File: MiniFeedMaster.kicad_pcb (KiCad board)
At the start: 2 copper layers, 58.4 x 83.2 mm, 120 parts, among them J1 SWD, J2 CAN, J3 UART, J4 USB, J5 Feeder, J6 Chain, J7 VIn, J8 I2C, J9 EXT, SW1 Button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

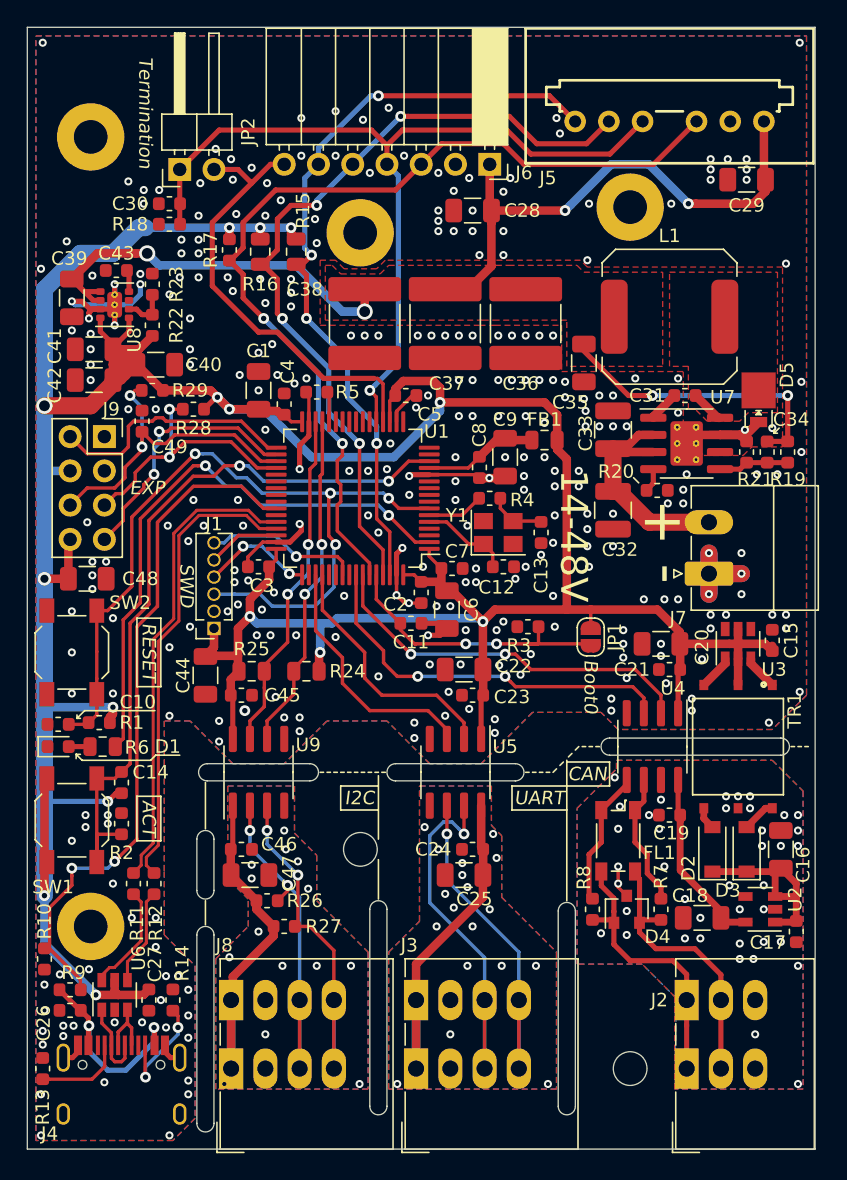
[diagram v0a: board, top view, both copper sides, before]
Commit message: Changed mounting holes from 2.5mm to 3mm Changed some 0.2mm vias to 0.3mm.
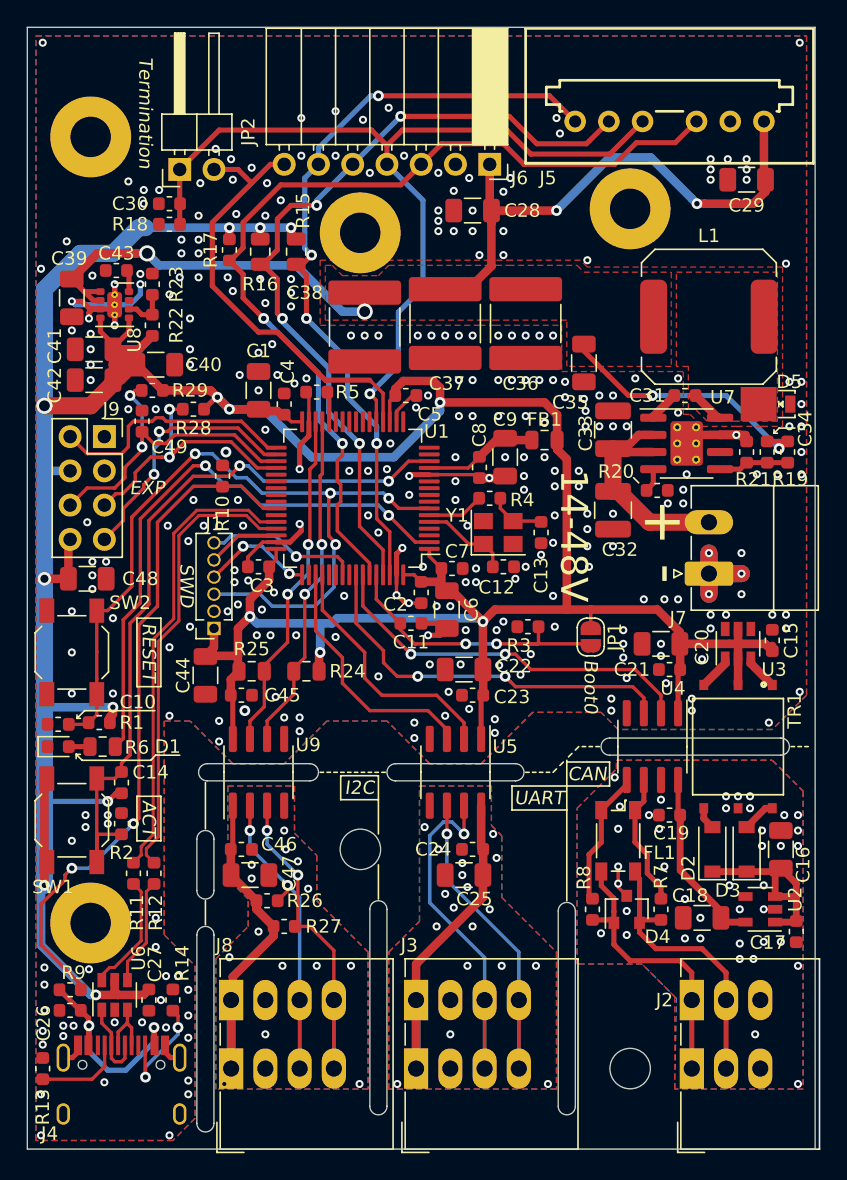
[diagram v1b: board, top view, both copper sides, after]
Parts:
- REF** (x4): value MountingHole_2.5mm_Pad -> MountingHole_3mm_Pad; footprint MountingHole:MountingHole_2.5mm_Pad -> MountingHole:MountingHole_3mm_Pad
- REF** (x2): value MountingHole_2.5mm -> MountingHole_3mm; footprint MountingHole:MountingHole_2.5mm -> MountingHole:MountingHole_3mm
- moved R10 38.2 mm to (219.6, 62.5), turned to 90 degrees
- moved L1 2.92 mm to (255.7, 50.7)
- moved D5 1.02 mm to (259.3, 57.1), turned to 0 degrees
- moved R11 0.76 mm to (213.0, 91.9)
- moved R12 0.76 mm to (214.5, 91.9)
- moved J2 0.38 mm to (254.4, 101.3)
- moved C38 0.25 mm to (230.1, 51.4)
- moved REF** 0.25 mm to (209.8, 95.6)
- moved REF** 0.13 mm to (249.8, 42.7)
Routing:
- net GND: track 72.7 -> 69.6 mm, vias 306 -> 305
- net /FD_FB: track 64.2 -> 65.7 mm
- net +12V: track 92.6 -> 91.1 mm
- net /USB_P: track 34.5 -> 33.7 mm
- net /USB_N: track 35.1 -> 34.3 mm
- net /USB/USB_R_P: track 7.52 -> 8.28 mm
- net /USB/USB_R_N: track 8.41 -> 9.17 mm
